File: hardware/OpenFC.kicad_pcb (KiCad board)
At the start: 8 copper layers, 37.6 x 37.6 mm, 253 parts, among them J1 5V, J10 5V, J11 5V, J12 5V, J13 5V, J14 5V, J15 5V, J16 5V, J17 5V, J18 5V, J19 5V, J2 5V, J20 5V, J21 5V, J22 5V, J23 5V, J24 5V, J25 5V, J26 5V, J27 5V, J28 5V, J29 5V, J3 5V, J30 5V, J31 5V, J32 5V, J33 5V, J34 5V, J35 5V, J36 5V, J38 5V, J39 5V, J4 5V, J40 5V, J41 5V, J42 5V, J43 5V, J44 5V, J45 5V, J46 5V, J47 5V, J48 5V, J49 5V, J5 5V, J50 5V, J51 5V, J52 5V, J53 5V, J54 5V, J55 5V, J56 5V, J57 5V, J58 5V, J59 5V, J6 5V, J7 5V, J8 5V, J9 5V, P1 SM08B-SRSS-TB(LF)(SN), Q1 DMN1150UFB-7B, Q2 DMN1150UFB-7B, Q7 DMN1150UFB-7B, SW12v1 TestPoint, SW5v1 TestPoint, U1 SM06B-SRSS-TB(LF)(SN), U11 PI3A223ZMEX, U12 WL9005D4-33, U13 TPS746-3.3DRV, U14 LSM6DSV16XTR, U15 XL-1010RGBC-WS2812B, U16 XL-1010RGBC-WS2812B, U17 XL-1010RGBC-WS2812B, U18 XL-1010RGBC-WS2812B, U19 XL-1010RGBC-WS2812B, U2 ESP32-C3FH4, U20 SX1281IMLTRT, U21 NCV8187AMT180TAG, U22 XL-1010RGBC-WS2812B, U23 XL-1010RGBC-WS2812B, U24 XL-1010RGBC-WS2812B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

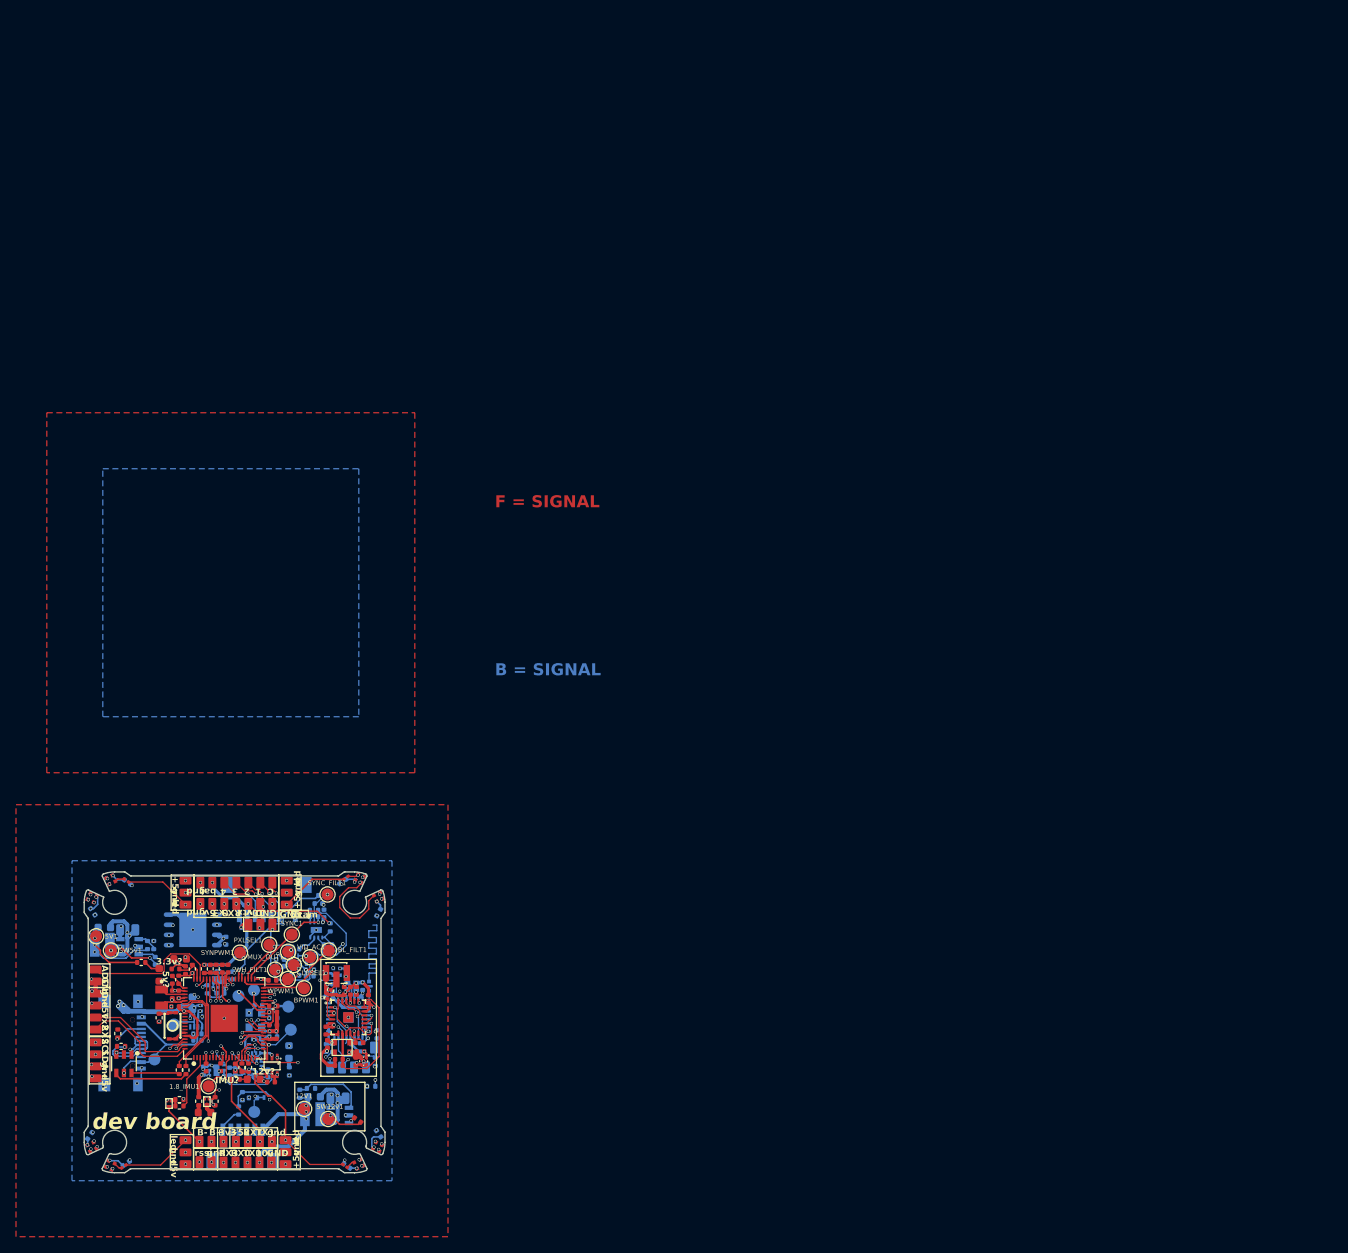
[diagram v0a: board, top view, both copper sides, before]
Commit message: switched to 0201
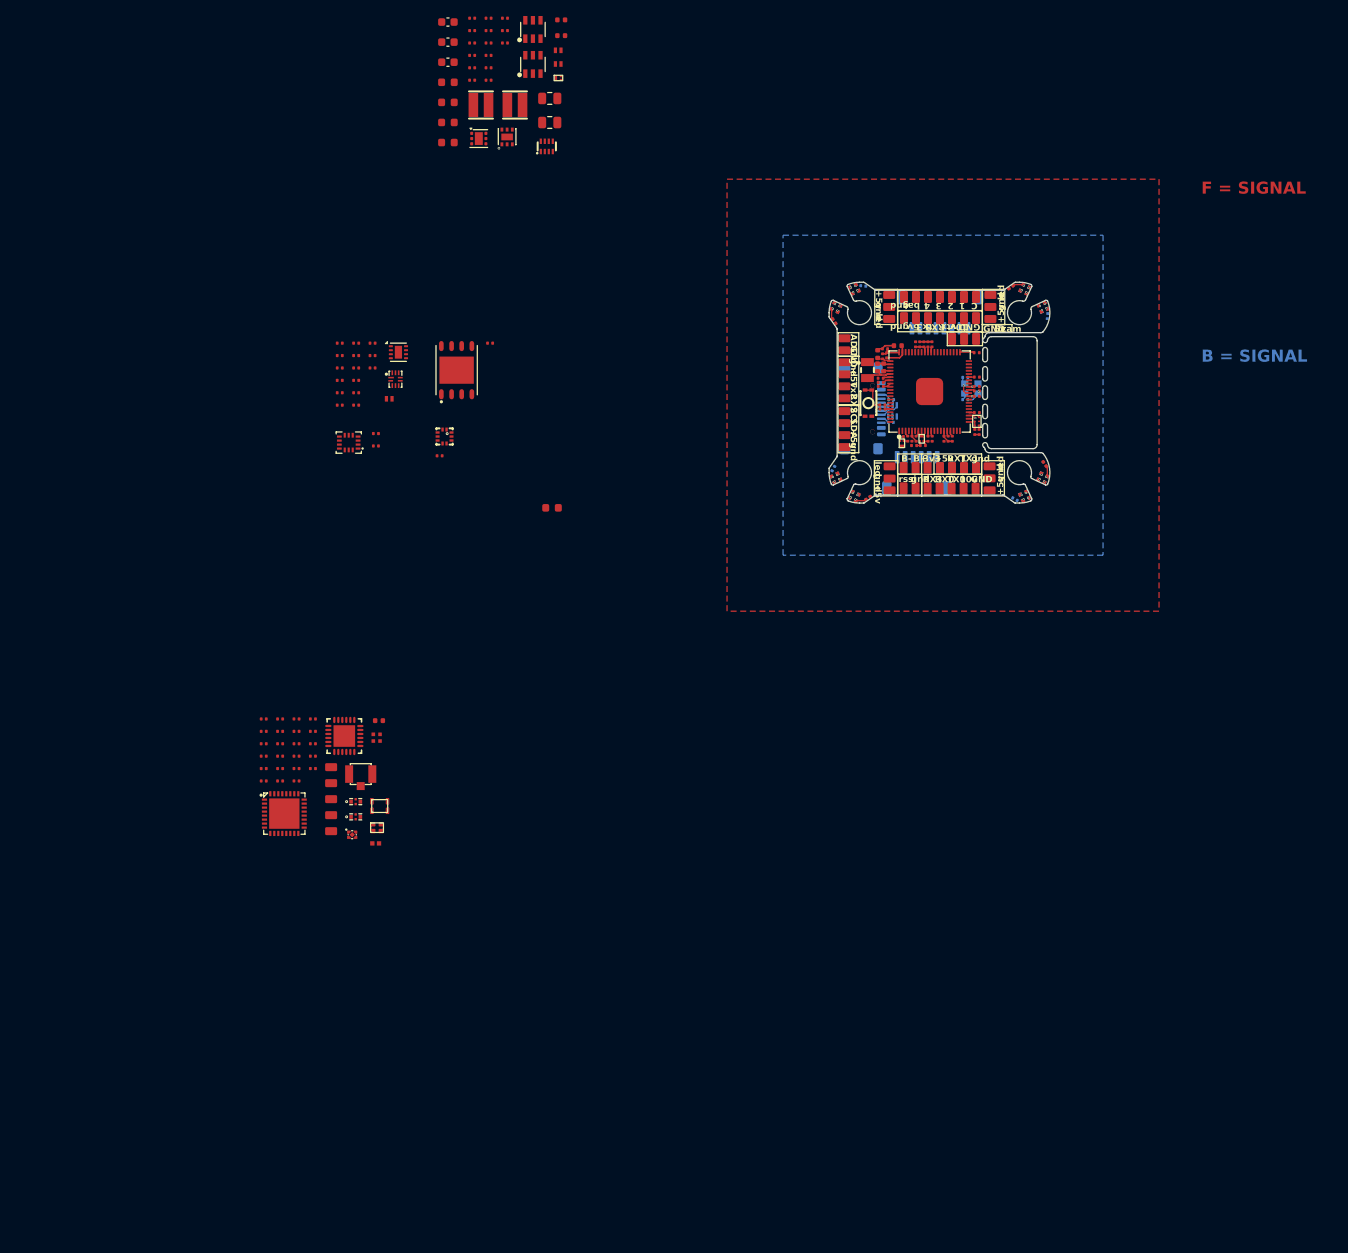
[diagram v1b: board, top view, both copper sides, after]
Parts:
- removed 1.8_IMU1, 12V1, 3v3CPU1, 5V1, 5V_PWR1, 5V_USB1, BL_FILT1, BPWM1, CLRSEL1, LEDLOW1, MUX_OUT1, PXLSEL1, SBUS1, SW12v1, SW5v1, SWC1, SWD1, SYNC1, SYNC_FILT1, SYNPWM1, VID_AC1, WH_FILT1, WPWM1: TestPoint, TestPoint:TestPoint_Pad_D1.5mm
- removed C111, C70, C72, C75, C76, C78, C79, C80, C81, C82, C83, C84, C85, C86, C87: 100n, Capacitor_SMD:C_0402_1005Metric
- removed C71, C77: 4.7uF, Capacitor_SMD:C_0402_1005Metric
- removed C74: 20p, Capacitor_SMD:C_0402_1005Metric
- removed R34: 1k, Resistor_SMD:R_0402_1005Metric
- removed R46: 100k, Resistor_SMD:R_0402_1005Metric
- removed R47, R54: 10k, Resistor_SMD:R_0402_1005Metric
- removed R48, R49: 30R, Resistor_SMD:R_0402_1005Metric
- removed R51, R52: 5.1k, Resistor_SMD:R_0402_1005Metric
- removed U41: TS2306A 240GF MSM 9_C2976675, lib:SW-SMD_4P-L3.0-W2.0-P0.85-LS3.5
- removed U42: TXU0101DCKR, lib:SC-70-6_L2.0-W1.3-P0.65-LS2.1-BL
- added C20: 100n, Capacitor_SMD:C_0201_0603Metric, F.Cu at (70.2, 133.5)
- added C21: 100n, Capacitor_SMD:C_0201_0603Metric, F.Cu at (70.2, 135.0)
- added C22: 100n, Capacitor_SMD:C_0201_0603Metric, F.Cu at (72.2, 127.3)
- added C23: 100n, Capacitor_SMD:C_0201_0603Metric, F.Cu at (72.2, 128.8)
- added C24: 100n, Capacitor_SMD:C_0201_0603Metric, F.Cu at (72.2, 130.4)
- added C25: 100n, Capacitor_SMD:C_0201_0603Metric, F.Cu at (72.2, 131.9)
- added C26: 100n, Capacitor_SMD:C_0201_0603Metric, F.Cu at (72.2, 133.5)
- added C27: 100n, Capacitor_SMD:C_0201_0603Metric, F.Cu at (157.2, 85.7)
- added C28: 100n, Capacitor_SMD:C_0201_0603Metric, F.Cu at (151.1, 80.5)
- added C29: 100n, Capacitor_SMD:C_0201_0603Metric, F.Cu at (151.2, 92.2)
- added C30: 100n, Capacitor_SMD:C_0201_0603Metric, F.Cu at (157.2, 87.0)
- added C31: 100n, Capacitor_SMD:C_0201_0603Metric, F.Cu at (145.2, 85.7)
- added C42: 100n, Capacitor_SMD:C_0201_0603Metric, F.Cu at (153.2, 92.2)
- added C43: 100n, Capacitor_SMD:C_0201_0603Metric, F.Cu at (149.1, 92.2)
- added C44: 100n, Capacitor_SMD:C_0201_0603Metric, F.Cu at (145.5, 88.5)
- added C54: 100n, Capacitor_SMD:C_0201_0603Metric, F.Cu at (157.0, 91.4)
- added C56: 100n, Capacitor_SMD:C_0201_0603Metric, F.Cu at (150.1, 80.5)
- added C59: 20p, Capacitor_SMD:C_0201_0603Metric, B.Cu at (155.8, 84.6)
- added C62: 4.7uF, Capacitor_SMD:C_0402_1005Metric, F.Cu at (144.9, 81.7)
- added C63: 100n, Capacitor_SMD:C_0201_0603Metric, F.Cu at (90.1, 94.4)
- added C65: 100n, Capacitor_SMD:C_0201_0603Metric, F.Cu at (145.8, 81.0)
- added R35: 10k, Capacitor_SMD:C_0201_0603Metric, F.Cu at (150.6, 80.5)
- added R36: 10k, Capacitor_SMD:C_0201_0603Metric, F.Cu at (157.3, 84.5)
- added R37: 30R, Capacitor_SMD:C_0201_0603Metric, F.Cu at (145.2, 84.7)
- added R38: 30R, Capacitor_SMD:C_0201_0603Metric, F.Cu at (145.2, 85.2)
- added R39: 5.1k, Capacitor_SMD:C_0201_0603Metric, B.Cu at (146.5, 87.4)
- added R41: 5.1k, Capacitor_SMD:C_0201_0603Metric, F.Cu at (154.2, 92.2)
- added R44: 10k, Capacitor_SMD:C_0201_0603Metric, F.Cu at (145.4, 88.0)
- added R9: 1k, Capacitor_SMD:C_0201_0603Metric, F.Cu at (74.3, 131.9)
- added U10: TXU0101DRYR, lib:SON-6_L1.5-W1.0-P0.50-TL, F.Cu at (157.3, 90.1)
- added U32: TS2306A 240GF MSM 9_C2976675, lib:SW-SMD_4P-L3.0-W2.0-P0.85-LS3.5, F.Cu at (143.7, 87.8)
- C1, C12, C13, C14, C15, C18, C19, C4, C46, C47, C5, C57, C58, C6, C7, C73, C8, C9: footprint Capacitor_SMD:C_0402_1005Metric -> Capacitor_SMD:C_0201_0603Metric
- C10, C11, C3, C32, C33, C34, C39, C41, C45, C49, C50, C51, C52, C53, C55, C61, C64: footprint Capacitor_SMD:C_0402_1005Metric -> Capacitor_SMD:C_0201_0603Metric; moved to F.Cu
- C16, C2, C35, C37, C38, C40, C48, D2, D21, D3, D6, FL2, J10, J11, J12, J26, J31, L3, L4, L7, Q2, U11, U13, U14, U19, U2, U21, U22, U26, U28, U30, U33, U37, U9, X2: moved to F.Cu
- C36: value 100nF -> 100n; footprint Capacitor_SMD:C_0402_1005Metric -> Capacitor_SMD:C_0201_0603Metric
- C60: value 100n -> 4.7uF
- D8: footprint lib:SOT-23-6_L2.9-W1.6-P0.95-LS2.8-BL -> Package_TO_SOT_SMD:SOT-666; moved to B.Cu
- R1, R10, R11, R14, R16, R17, R18, R2, R20, R21, R22, R23, R24, R25, R26, R28, R3, R30, R31, R4, R6, R7, R8: footprint Resistor_SMD:R_0402_1005Metric -> Capacitor_SMD:C_0201_0603Metric; moved to F.Cu
- R12, R13, R15, R19, R5, R55, R56: footprint Resistor_SMD:R_0402_1005Metric -> Capacitor_SMD:C_0201_0603Metric
- R27, R32: value 33R -> 30R; footprint Resistor_SMD:R_0402_1005Metric -> Capacitor_SMD:C_0201_0603Metric; moved to F.Cu
- R29: value 470 -> 470R; footprint Resistor_SMD:R_0402_1005Metric -> Capacitor_SMD:C_0201_0603Metric
- R33: value 100R -> 75R; footprint Resistor_SMD:R_0402_1005Metric -> Capacitor_SMD:C_0201_0603Metric; moved to F.Cu
- R40: value 10k -> 5.1k; footprint Resistor_SMD:R_0402_1005Metric -> Capacitor_SMD:C_0201_0603Metric; moved to B.Cu
- R42: value 6.8k -> 5.1k; footprint Resistor_SMD:R_0402_1005Metric -> Capacitor_SMD:C_0201_0603Metric
- R43: value 6.8k -> 100k; footprint Resistor_SMD:R_0402_1005Metric -> Capacitor_SMD:C_0201_0603Metric
- U16, U18, U4: moved to B.Cu
- U6, U7: value LMR51420YDDCR -> LMR51420YFDDCR; moved to F.Cu
- moved C47 145.9 mm to (165.7, 95.4), turned to 125 degrees
- moved U26 140.5 mm to (139.7, 75.8), turned to -115 degrees
- moved U27 140.2 mm to (139.7, 75.8), turned to -25 degrees
- moved U25 139.9 mm to (165.5, 75.8), turned to -65 degrees
- moved U8 139.9 mm to (165.5, 75.8), turned to -155 degrees
- moved C46 138.7 mm to (162.0, 99.8), turned to 150 degrees
- moved R12 138.6 mm to (96.2, 41.2), turned to 0 degrees
- moved U6 137.9 mm to (101.8, 41.1), turned to 0 degrees
- moved C2 137.8 mm to (105.3, 39.9), turned to 0 degrees
- moved U24 136.0 mm to (163.3, 73.5), turned to -115 degrees
- moved U5 136.0 mm to (163.3, 73.5), turned to 155 degrees
- moved R28 136.0 mm to (98.3, 39.7)
- moved C36 135.4 mm to (94.2, 42.8), turned to 0 degrees
- moved C38 135.4 mm to (91.1, 40.2)
- moved R29 135.3 mm to (98.3, 41.2)
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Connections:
- C10 pad 1: GND -> Net-(U37B--)
- C10 pad 2: Net-(U37B--) -> GND
- C3 pad 1: GND -> /OSD/VBLACK_FILT
- C3 pad 2: /OSD/VBLACK_FILT -> GND
- C50 pad 1: Net-(C50-Pad1) -> +3.3V
- C51 pad 1: +3.3V_ELRS -> +3.3V
- C52 pad 1: +3.3V_ELRS -> +3.3V
- C53 pad 1: +3.3V_ELRS -> +3.3V
- C60 pad 1: +3.3V_ELRS -> Net-(U36-ADC_AVDD)
- C64 pad 1: GND -> /OSD/VWHITE_FILT
- C64 pad 2: /OSD/VWHITE_FILT -> GND
- L7 pad 2: Net-(C50-Pad1) -> Net-(C25-Pad1)
- R10 pad 1: /OSD/OSD_VBLACK_PWM -> /OSD/OSD_SYNCLVL_PWM
- R10 pad 2: /OSD/VBLACK_FILT -> Net-(U37B--)
- R13 pad 1: /RP2350A/BEEPER -> Net-(Q7-G)
- R13 pad 2: Net-(Q7-G) -> /RP2350A/BEEPER
- R19 pad 1: +5V -> /POWER/1.8V_PG
- R19 pad 2: /POWER/1.8V_PG -> +5V
- R21 pad 1: /OSD/OSD_SYNCLVL_PWM -> /OSD/OSD_VBLACK_PWM
- R21 pad 2: Net-(U37B--) -> /OSD/VBLACK_FILT
- R22 pad 1: Net-(D6-A) -> /RP2350A/LED0
- R22 pad 2: /RP2350A/LED0 -> Net-(D6-A)
- R23 pad 1: Net-(C73-Pad2) -> /RP2350A/XOUT
- R23 pad 2: /RP2350A/XOUT -> Net-(C73-Pad2)
- R25 pad 1: /OSD/OSD_SYNC_RAW -> Net-(U37B-+)
- R25 pad 2: Net-(U37B-+) -> /OSD/OSD_SYNC_RAW
- R27 pad 1: /OSD/VIDEO_IN -> /OSD/VID_IN
- R27 pad 2: /OSD/VID_IN -> /OSD/VIDEO_IN
- R40 pad 2: Net-(R40-Pad2) -> Net-(USB1-CC1)
- R42 pad 1: +3.3V -> /I2C_SDA
- R42 pad 2: /I2C_SCL -> +3.3V
- R43 pad 1: +3.3V -> +BATT
- R43 pad 2: /I2C_SDA -> /RP2350A/ADC_VBAT
- R7 pad 1: +5V_BUCK -> Net-(U33-PR1)
- R7 pad 2: Net-(U33-PR1) -> +5V_BUCK
- U15 pad 4: Net-(JP1-B) -> Net-(U15-DIN)
- U16 pad 1: Net-(U16-DOUT) -> unconnected-(U16-DOUT-Pad1)
- U18 pad 1: Net-(U18-DOUT) -> unconnected-(U18-DOUT-Pad1)
- U2 pad 2: Net-(C50-Pad1) -> Net-(C25-Pad1)
- U2 pad 3: Net-(C50-Pad1) -> Net-(C25-Pad1)
- U22 pad 4: Net-(U22-DIN) -> Net-(U17-DOUT)
- U23 pad 4: Net-(U23-DIN) -> Net-(U22-DOUT)
- U26 pad 4: Net-(U15-DOUT) -> Net-(JP4-B)
- U27 pad 4: Net-(U16-DOUT) -> Net-(U26-DOUT)
- U28 pad 4: Net-(U17-DOUT) -> Net-(U26-DOUT)
- U29 pad 4: Net-(U18-DOUT) -> Net-(U28-DOUT)
- U3 pad 1: Net-(U22-DIN) -> Net-(U15-DIN)
- U3 pad 4: Net-(JP4-B) -> Net-(JP1-B)
- U36 pad 33: Net-(U36-SWCLK) -> unconnected-(U36-SWCLK-Pad33)
- U36 pad 34: Net-(U36-SWDIO) -> unconnected-(U36-SWDIO-Pad34)
- U36 pad 9: unconnected-(U36-GPIO11-Pad9) -> /POWER/10V_ENABLE
- U4 pad 1: Net-(U23-DIN) -> unconnected-(U4-DOUT-Pad1)
- U4 pad 4: Net-(U22-DIN) -> Net-(U15-DIN)
- U6 pad 5: +BATT -> /POWER/10V_ENABLE
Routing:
- net /LED: track 117.8 -> 0.16 mm, vias 4 -> 1
- net GND: track 101.9 -> 9.44 mm, vias 91 -> 11
- net +BATT: track 81.2 -> 0.00 mm, vias 7 -> 0
- net +5V: track 69.3 -> 1.03 mm, vias 32 -> 8
- net +3.3V: track 79.7 -> 13.2 mm, vias 18 -> 1
- net +12V: track 55.0 -> 0.00 mm, vias 6 -> 0
- net /UART1_TX: track 47.9 -> 0.00 mm, vias 4 -> 0
- net /UART1_RX: track 45.6 -> 0.00 mm, vias 4 -> 0
- net +5V_BUCK: track 39.2 -> 0.00 mm, vias 4 -> 0
- net +1.1V: track 33.3 -> 5.93 mm, vias 4 -> 1
- net /I2C_SDA: track 27.0 -> 0.72 mm, vias 2 -> 0
- net /I2C_SCL: track 26.9 -> 0.77 mm, vias 2 -> 0
- net /PADS/RSSI: track 23.9 -> 0.00 mm, vias 2 -> 0
- net /PADS/M4: track 23.3 -> 0.00 mm, vias 2 -> 0
- net /ELRS/ESP8285_EN: track 22.8 -> 0.00 mm, vias 2 -> 0
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- removed copper zone on In3.Cu, net +3.3V
- removed copper zone on In3.Cu, net +3.3V_ELRS
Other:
- board size 37.6 x 37.6 mm -> 27.6 x 27.6 mm
- board text removed: "12v?"
- board text removed: "3.3v?"
- board text removed: "5V"
- board text removed: "5v?"
- board text removed: "IMU?"
- board text removed: "OPENFC"
- board text removed: "RX"
- board text removed: "TX"
- board text removed: "dev board"
